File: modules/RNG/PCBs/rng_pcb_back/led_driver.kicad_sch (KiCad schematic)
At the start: 4 parts, among them U1 TLC5940NT, U6 TLC5940PWP

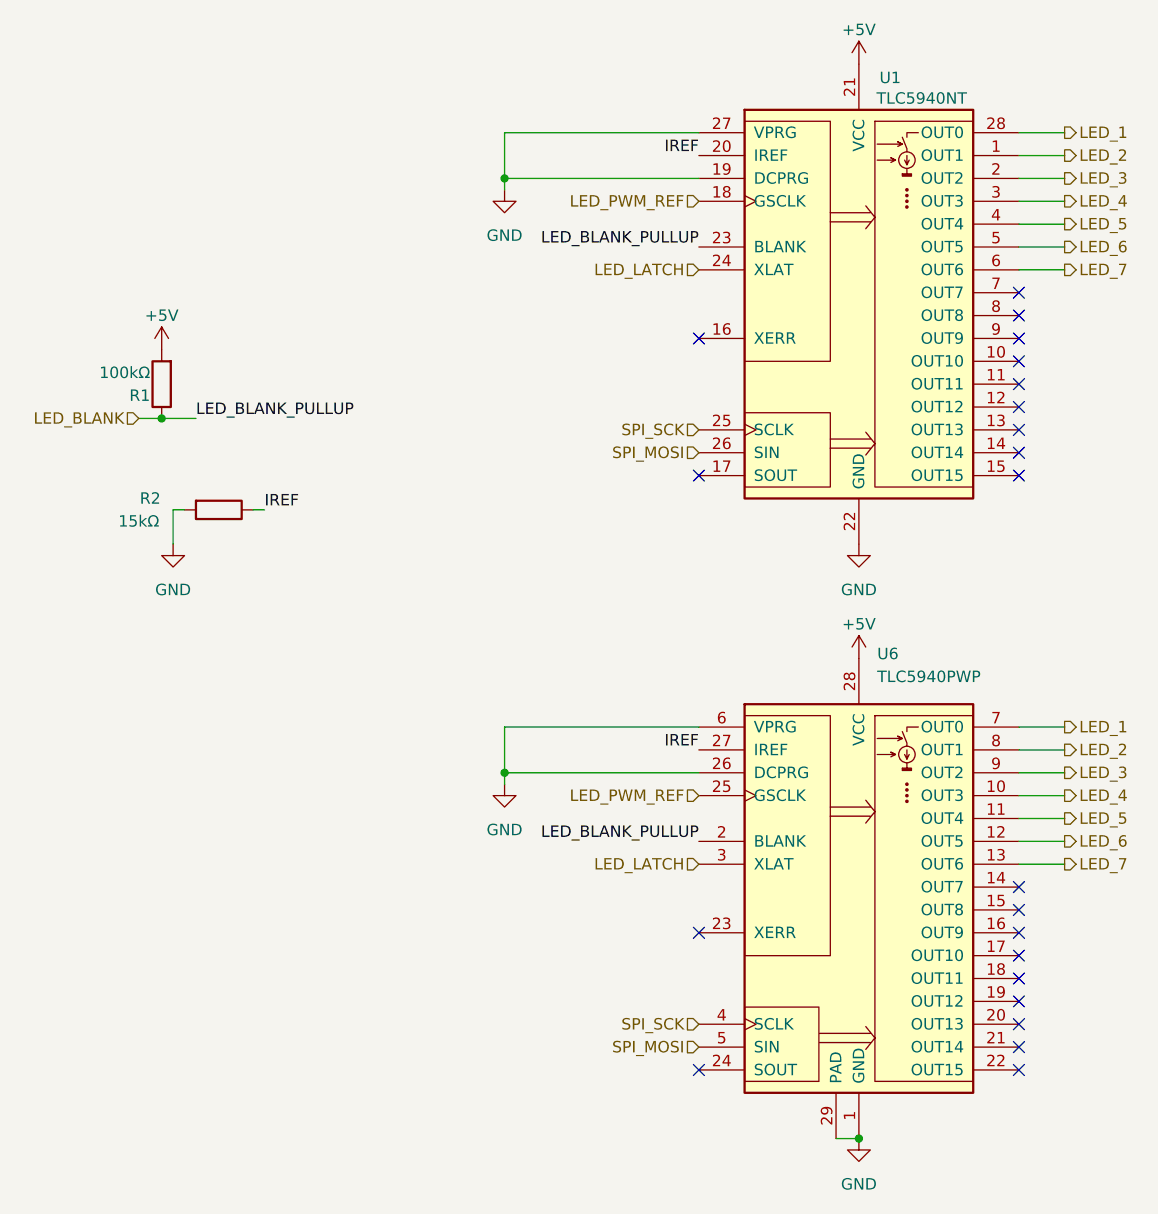
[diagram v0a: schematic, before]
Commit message: Fix #55 and add decoupling capacitors
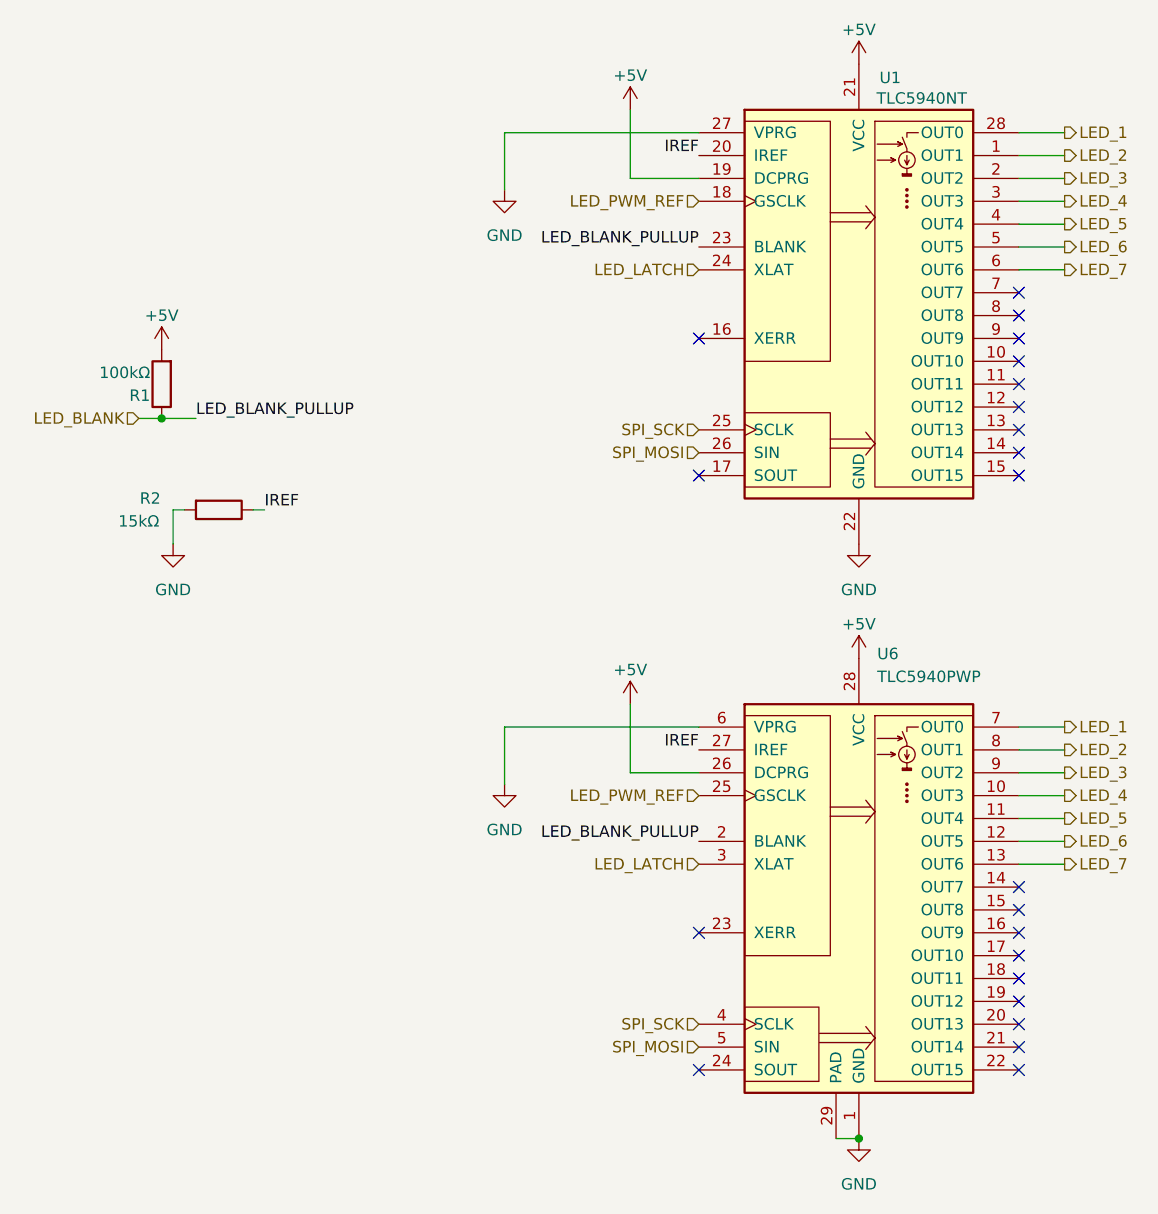
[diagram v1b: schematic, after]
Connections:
- net +5V: now also U1.19 (DCPRG), U6.26 (DCPRG)
- net GND: no longer U1.19 (DCPRG), U6.26 (DCPRG)
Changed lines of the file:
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@@
-	)
-	(junction
-		(at 74.93 116.84)
-		(diameter 0)
-		(color 0 0 0 0)
 	)
 	(junction
@@
 		(color 0 0 0 0)
 	)
-	(junction
-		(at 74.93 50.8)
-		(diameter 0)
-		(color 0 0 0 0)
-	)
 	(no_connect
 		(at 132.08 139.7)
@@
 	(wire
 		(pts
-			(xy 74.93 50.8) (xy 96.52 50.8)
-		)
-		(stroke
-			(width 0)
-			(type default)
-		)
-	)
-	(wire
-		(pts
 			(xy 36.83 77.47) (xy 40.64 77.47)
 		)
@@
 	(wire
 		(pts
-			(xy 74.93 116.84) (xy 96.52 116.84)
+			(xy 88.9 50.8) (xy 96.52 50.8)
 		)
 		(stroke
@@
 	(wire
 		(pts
-			(xy 74.93 111.76) (xy 74.93 116.84)
-		)
-		(stroke
-			(width 0)
-			(type default)
-		)
-	)
-	(wire
-		(pts
-			(xy 74.93 50.8) (xy 74.93 52.07)
+			(xy 74.93 111.76) (xy 74.93 118.11)
+		)
+		(stroke
+			(width 0)
+			(type default)
+		)
+	)
+	(wire
+		(pts
+			(xy 74.93 45.72) (xy 74.93 52.07)
 		)
 		(stroke
@@
 	(wire
 		(pts
+			(xy 88.9 116.84) (xy 96.52 116.84)
+		)
+		(stroke
+			(width 0)
+			(type default)
+		)
+	)
+	(wire
+		(pts
 			(xy 132.08 45.72) (xy 137.16 45.72)
 		)
@@
 	(wire
 		(pts
+			(xy 88.9 109.22) (xy 88.9 116.84)
+		)
+		(stroke
+			(width 0)
+			(type default)
+		)
+	)
+	(wire
+		(pts
 			(xy 132.08 119.38) (xy 137.16 119.38)
 		)
@@
 	(wire
 		(pts
-			(xy 74.93 45.72) (xy 74.93 50.8)
+			(xy 88.9 43.18) (xy 88.9 50.8)
 		)
 		(stroke
@@
 		(pts
 			(xy 132.08 127) (xy 137.16 127)
-		)
-		(stroke
-			(width 0)
-			(type default)
-		)
-	)
-	(wire
-		(pts
-			(xy 74.93 116.84) (xy 74.93 118.11)
 		)
 		(stroke
@@
 	)
 	(symbol
+		(lib_id "power:+5V")
+		(at 88.9 109.22 0)
+		(unit 1)
+		(exclude_from_sim no)
+		(in_bom yes)
+		(on_board yes)
+		(dnp no)
+		(fields_autoplaced yes)
+		(property "Reference" "#PWR048"
+			(at 88.9 113.03 0)
+			(effects
+				(font
+					(size 1.27 1.27)
+				)
+				(hide yes)
+			)
+		)
+		(property "Value" "+5V"
+			(at 88.9 105.41 0)
+			(effects
+				(font
+					(size 1.27 1.27)
+				)
+			)
+		)
+		(property "Footprint" ""
+			(at 88.9 109.22 0)
+			(effects
+				(font
+					(size 1.27 1.27)
+				)
+				(hide yes)
+			)
+		)
+		(property "Datasheet" ""
+			(at 88.9 109.22 0)
+			(effects
+				(font
+					(size 1.27 1.27)
+				)
+				(hide yes)
+			)
+		)
+		(property "Description" ""
+			(at 88.9 109.22 0)
+			(effects
+				(font
+					(size 1.27 1.27)
+				)
+				(hide yes)
+			)
+		)
+		(pin "1"
+		)
+		(instances
+			(project "rng_pcb_back"
+				(path "/92d63849-2602-44c9-baaa-01c9094be14f/5cf0a259-bdf3-44a9-9c89-339d20abf95a"
+					(reference "#PWR048")
+					(unit 1)
+				)
+			)
+		)
+	)
+	(symbol
 		(lib_id "power:GND")
 		(at 74.93 118.11 0)
@@
 					(unit 1)
 				)
+			)
+		)
+	)
+	(symbol
+		(lib_id "power:+5V")
+		(at 88.9 43.18 0)
+		(unit 1)
+		(exclude_from_sim no)
+		(in_bom yes)
+		(on_board yes)
+		(dnp no)
+		(fields_autoplaced yes)
+		(property "Reference" "#PWR049"
+			(at 88.9 46.99 0)
+			(effects
+				(font
+					(size 1.27 1.27)
+				)
+				(hide yes)
+			)
+		)
+		(property "Value" "+5V"
+			(at 88.9 39.37 0)
+			(effects
+				(font
+					(size 1.27 1.27)
+				)
+			)
+		)
+		(property "Footprint" ""
+			(at 88.9 43.18 0)
+			(effects
+				(font
+					(size 1.27 1.27)
+				)
+				(hide yes)
+			)
+		)
+		(property "Datasheet" ""
+			(at 88.9 43.18 0)
+			(effects
+				(font
+					(size 1.27 1.27)
+				)
+				(hide yes)
+			)
+		)
+		(property "Description" ""
+			(at 88.9 43.18 0)
+			(effects
+				(font
+					(size 1.27 1.27)
+				)
+				(hide yes)
+			)
+		)
+		(pin "1"
+		)
+		(instances
+			(project "rng_pcb_back"
+				(path "/92d63849-2602-44c9-baaa-01c9094be14f/5cf0a259-bdf3-44a9-9c89-339d20abf95a"
+					(reference "#PWR049")
+					(unit 1)
+				)

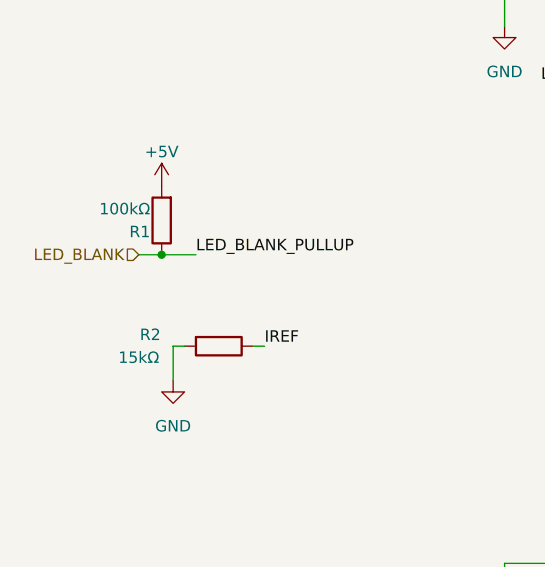
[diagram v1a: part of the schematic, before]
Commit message: Fix wrong resistor designators on RNG
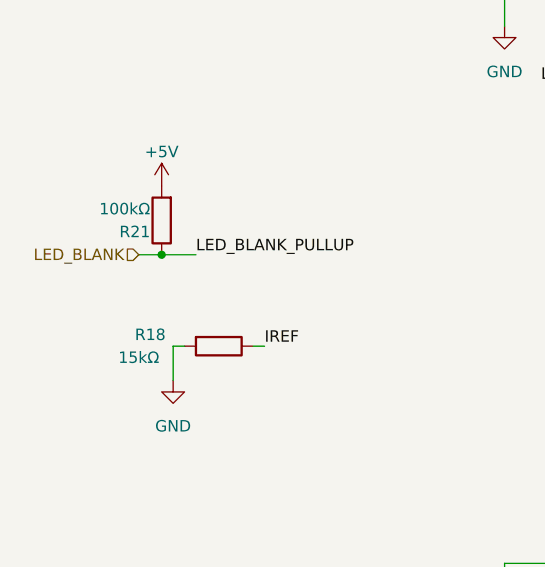
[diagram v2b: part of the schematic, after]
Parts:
- renumbered R2 to R18, R1 to R21
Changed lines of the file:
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@@
 		(on_board yes)
 		(dnp no)
-		(property "Reference" "R1"
+		(property "Reference" "R21"
 			(at 35.56 74.93 0)
 			(effects
@@
 			(project "rng_pcb_back"
 				(path "/92d63849-2602-44c9-baaa-01c9094be14f/5cf0a259-bdf3-44a9-9c89-339d20abf95a"
-					(reference "R1")
+					(reference "R21")
 					(unit 1)
 				)
@@
 		(on_board yes)
 		(dnp no)
-		(property "Reference" "R2"
+		(property "Reference" "R18"
 			(at 35.56 86.36 90)
 			(effects
@@
 			(project "rng_pcb_back"
 				(path "/92d63849-2602-44c9-baaa-01c9094be14f/5cf0a259-bdf3-44a9-9c89-339d20abf95a"
-					(reference "R2")
-					(unit 1)
-				)
+					(reference "R18")
+					(unit 1)
+				)
